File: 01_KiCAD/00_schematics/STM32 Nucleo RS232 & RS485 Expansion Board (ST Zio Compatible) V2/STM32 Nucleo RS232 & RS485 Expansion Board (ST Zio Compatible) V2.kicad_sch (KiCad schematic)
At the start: 0 parts

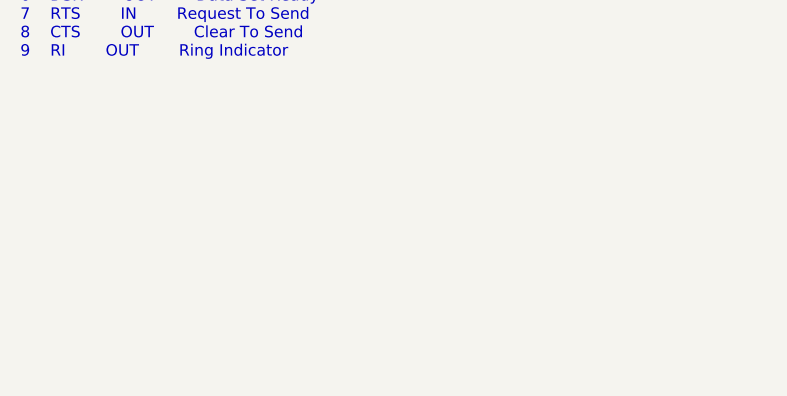
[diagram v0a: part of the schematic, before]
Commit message: Added components
Added R1 - R4 0R pass-through resistors for RS485 data lines to seperate them from RS232 Net
Added capacitors C1+ and C2+ for charge pump
Completed table on root page for THVD4431 and ZIO Connector Pin Layout
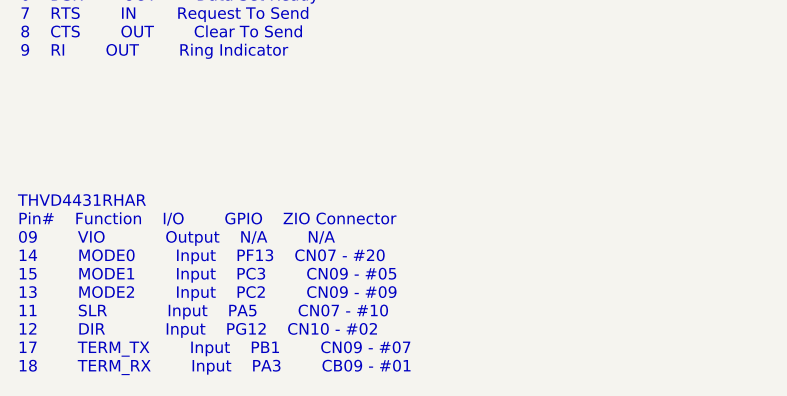
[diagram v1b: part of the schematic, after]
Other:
- note added: "THVD4431RHAR Pin# Function I/O GPIO ZIO Connector 09 VIO Output N/A N/A 14 MODE0 Input PF13 CN07 - #20 15 MODE1 Input PC3 CN09 - #05 13 MODE2 Input PC2 CN09 - #09 11 SLR Input PA5 CN07 - #10 12 DIR Input PG12 CN10 - #02 17 TERM_TX Input PB1 CN09 - #07 18 TERM_RX Input PA3 CB09 - #01"
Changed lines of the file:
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@@
+		)
+	)
+	(text "THVD4431RHAR\nPin#	Function	I/O		GPIO	ZIO Connector\n09		VIO			Output	N/A		N/A\n14		MODE0		Input	PF13	CN07 - #20\n15		MODE1		Input	PC3		CN09 - #05\n13		MODE2		Input	PC2		CN09 - #09\n11		SLR			Input	PA5		CN07 - #10\n12		DIR			Input	PG12	CN10 - #02\n17		TERM_TX		Input	PB1		CN09 - #07\n18		TERM_RX		Input	PA3		CB09 - #01\n"
+		(exclude_from_sim no)
+		(at 20.574 116.332 0)
+		(effects
+			(font
+				(size 1.27 1.27)
+			)
+			(justify left top)
 		)
 	)

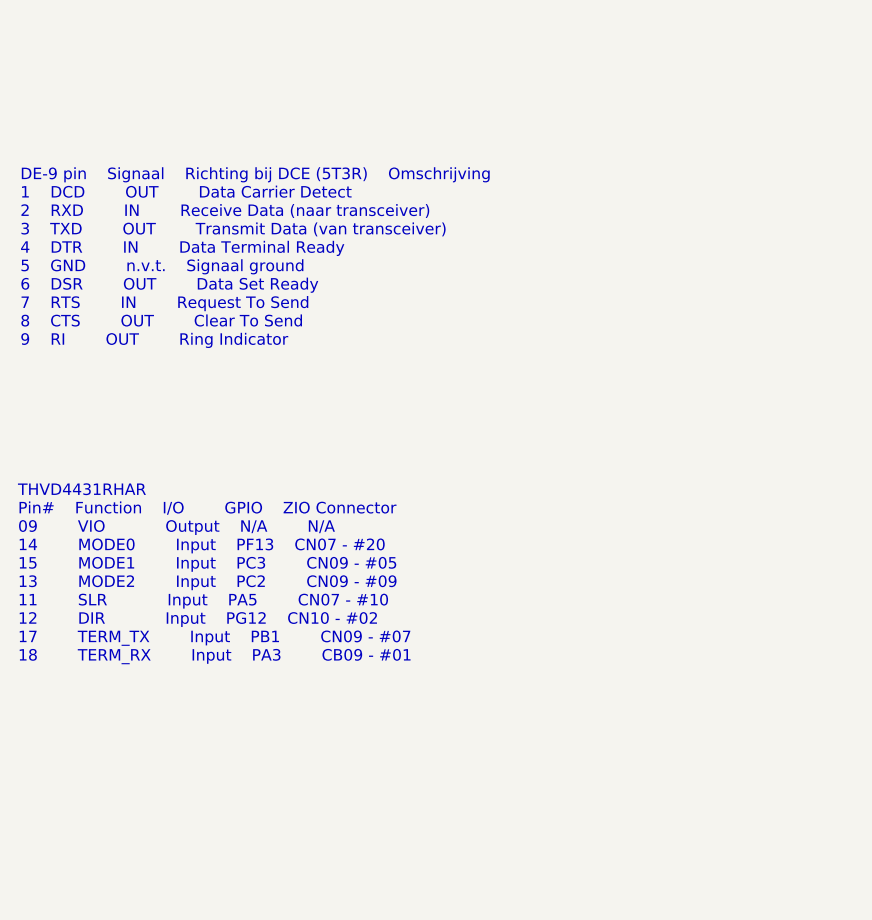
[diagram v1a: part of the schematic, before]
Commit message: Complemented descriptions
Complemented the RS232, RS485 and THVD4431 description table on the Root page
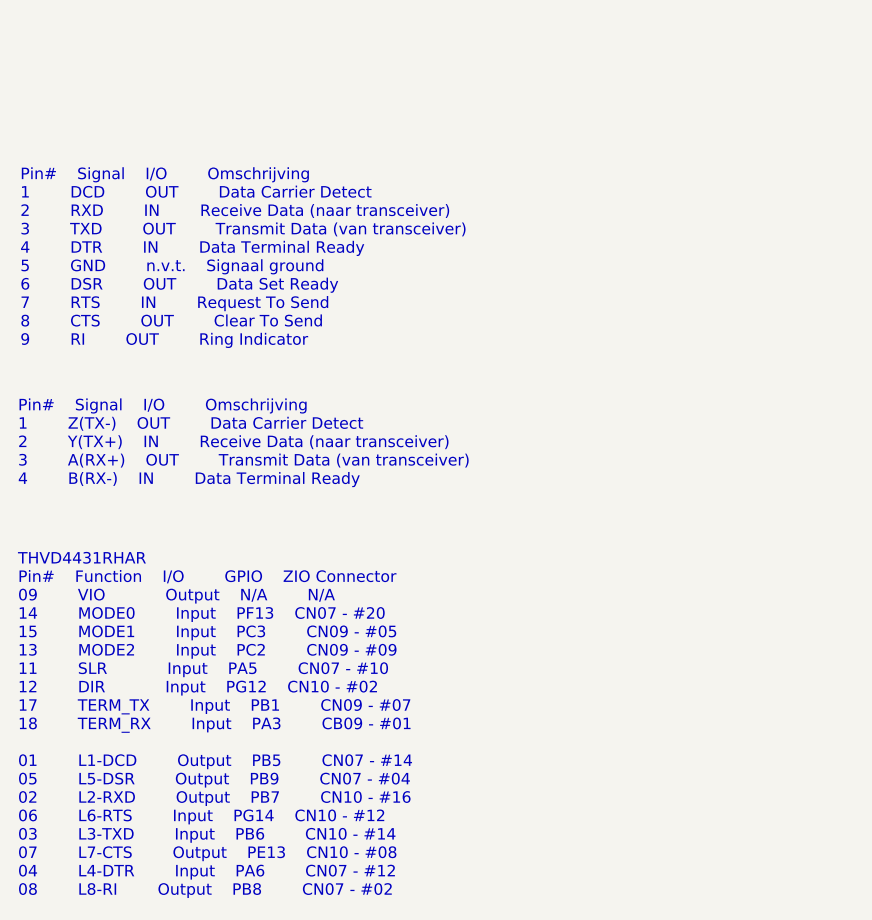
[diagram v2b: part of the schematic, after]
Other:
- note added: "Pin# Signal I/O Omschrijving 1 DCD OUT Data Carrier Detect 2 RXD IN Receive Data (naar transceiver) 3 TXD OUT Transmit Data (van transceiver) 4 DTR IN Data Terminal Ready 5 GND n.v.t. Signaal ground 6 DSR OUT Data Set Ready 7 RTS IN Request To Send 8 CTS OUT Clear To Send 9 RI OUT Ring Indicator"
- note added: "Pin# Signal I/O Omschrijving 1 Z(TX-) OUT Data Carrier Detect 2 Y(TX+) IN Receive Data (naar transceiver) 3 A(RX+) OUT Transmit Data (van transceiver) 4 B(RX-) IN Data Terminal Ready"
- note added: "THVD4431RHAR Pin# Function I/O GPIO ZIO Connector 09 VIO Output N/A N/A 14 MODE0 Input PF13 CN07 - #20 15 MODE1 Input PC3 CN09 - #05 13 MODE2 Input PC2 CN09 - #09 11 SLR Input PA5 CN07 - #10 12 DIR Input PG12 CN10 - #02 17 TERM_TX Input PB1 CN09 - #07 18 TERM_RX Input PA3 CB09 - #01 01 L1-DCD Output PB5 CN07 - #14 05 L5-DSR Output PB9 CN07 - #04 02 L2-RXD Output PB7 CN10 - #16 06 L6-RTS Input PG1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"
- note removed: "DE-9 pin Signaal Richting bij DCE (5T3R) Omschrijving 1 DCD OUT Data Carrier Detect 2 RXD IN Receive Data (naar transceiver) 3 TXD OUT Transmit Data (van transceiver) 4 DTR IN Data Terminal Ready 5 GND n.v.t. Signaal ground 6 DSR OUT Data Set Ready 7 RTS IN Request To Send 8 CTS OUT Clear To Send 9 RI OUT Ring Indicator"
- note removed: "THVD4431RHAR Pin# Function I/O GPIO ZIO Connector 09 VIO Output N/A N/A 14 MODE0 Input PF13 CN07 - #20 15 MODE1 Input PC3 CN09 - #05 13 MODE2 Input PC2 CN09 - #09 11 SLR Input PA5 CN07 - #10 12 DIR Input PG12 CN10 - #02 17 TERM_TX Input PB1 CN09 - #07 18 TERM_RX Input PA3 CB09 - #01"
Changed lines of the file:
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@@
 		(comment 3 "Initial revision")
 	)
-	(text "DE-9 pin	Signaal	Richting bij DCE (5T3R)	Omschrijving\n1	DCD		OUT		Data Carrier Detect\n2	RXD		IN		Receive Data (naar transceiver)\n3	TXD		OUT		Transmit Data (van transceiver)\n4	DTR		IN		Data Terminal Ready\n5	GND		n.v.t.	Signaal ground\n6	DSR		OUT		Data Set Ready\n7	RTS		IN		Request To Send\n8	CTS		OUT		Clear To Send\n9	RI		OUT		Ring Indicator"
+	(text "Pin#	Signal	I/O		Omschrijving\n1		DCD		OUT		Data Carrier Detect\n2		RXD		IN		Receive Data (naar transceiver)\n3		TXD		OUT		Transmit Data (van transceiver)\n4		DTR		IN		Data Terminal Ready\n5		GND		n.v.t.	Signaal ground\n6		DSR		OUT		Data Set Ready\n7		RTS		IN		Request To Send\n8		CTS		OUT		Clear To Send\n9		RI		OUT		Ring Indicator"
 		(exclude_from_sim no)
 		(at 20.828 91.186 0)
@@
 		)
 	)
-	(text "THVD4431RHAR\nPin#	Function	I/O		GPIO	ZIO Connector\n09		VIO			Output	N/A		N/A\n14		MODE0		Input	PF13	CN07 - #20\n15		MODE1		Input	PC3		CN09 - #05\n13		MODE2		Input	PC2		CN09 - #09\n11		SLR			Input	PA5		CN07 - #10\n12		DIR			Input	PG12	CN10 - #02\n17		TERM_TX		Input	PB1		CN09 - #07\n18		TERM_RX		Input	PA3		CB09 - #01\n"
+	(text "Pin#	Signal	I/O		Omschrijving\n1		Z(TX-)	OUT		Data Carrier Detect\n2		Y(TX+)	IN		Receive Data (naar transceiver)\n3		A(RX+)	OUT		Transmit Data (van transceiver)\n4		B(RX-)	IN		Data Terminal Ready\n"
 		(exclude_from_sim no)
-		(at 20.574 116.332 0)
+		(at 20.574 111.76 0)
 		(effects
 			(font
+				(size 1.27 1.27)
+			)
+			(justify left)
+		)
+	)
+	(text "THVD4431RHAR\nPin#	Function	I/O		GPIO	ZIO Connector\n09		VIO			Output	N/A		N/A\n14		MODE0		Input	PF13	CN07 - #20\n15		MODE1		Input	PC3		CN09 - #05\n13		MODE2		Input	PC2		CN09 - #09\n11		SLR			Input	PA5		CN07 - #10\n12		DIR			Input	PG12	CN10 - #02\n17		TERM_TX		Input	PB1		CN09 - #07\n18		TERM_RX		Input	PA3		CB09 - #01\n\n01		L1-DCD		Output	PB5		CN07 - #14\n05		L5-DSR		Output	PB9		CN07 - #04\n02		L2-RXD		Output	PB7		CN10 - #16\n06		L6-RTS		Input	PG14	CN10 - #12\n03		L3-TXD		Input	PB6		CN10 - #14\n07		L7-CTS		Output	PE13	CN10 - #08\n04		L4-DTR		Input	PA6		CN07 - #12\n08		L8-RI		Output	PB8		CN07 - #02"
+		(exclude_from_sim no)
+		(at 20.574 123.952 0)
+		(effects
+			(font

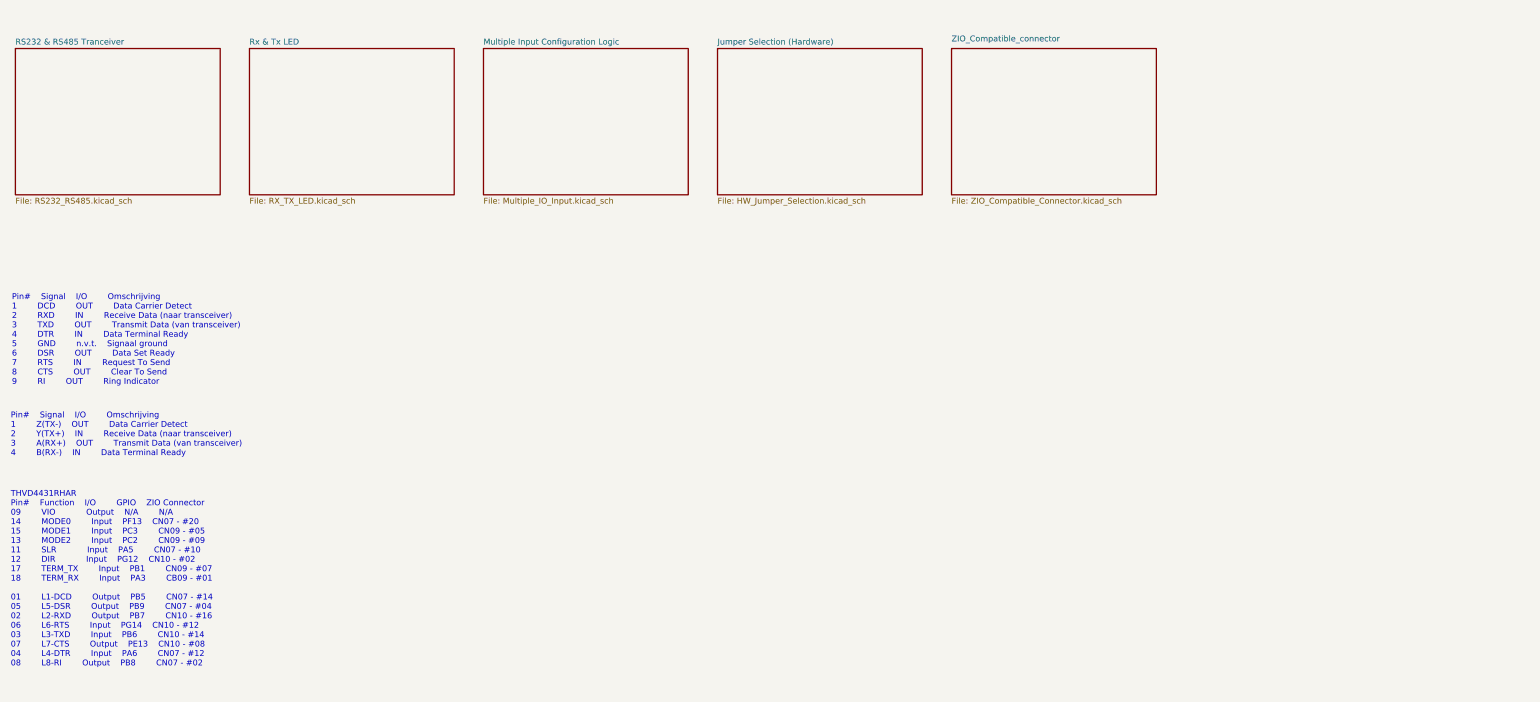
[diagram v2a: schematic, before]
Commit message: Added Dual Voltage Input
Added Dual Voltage Auto Select Input drawings. Added new hierarchical sheet with new pagenumber one. All other pages have been moved up by 1.
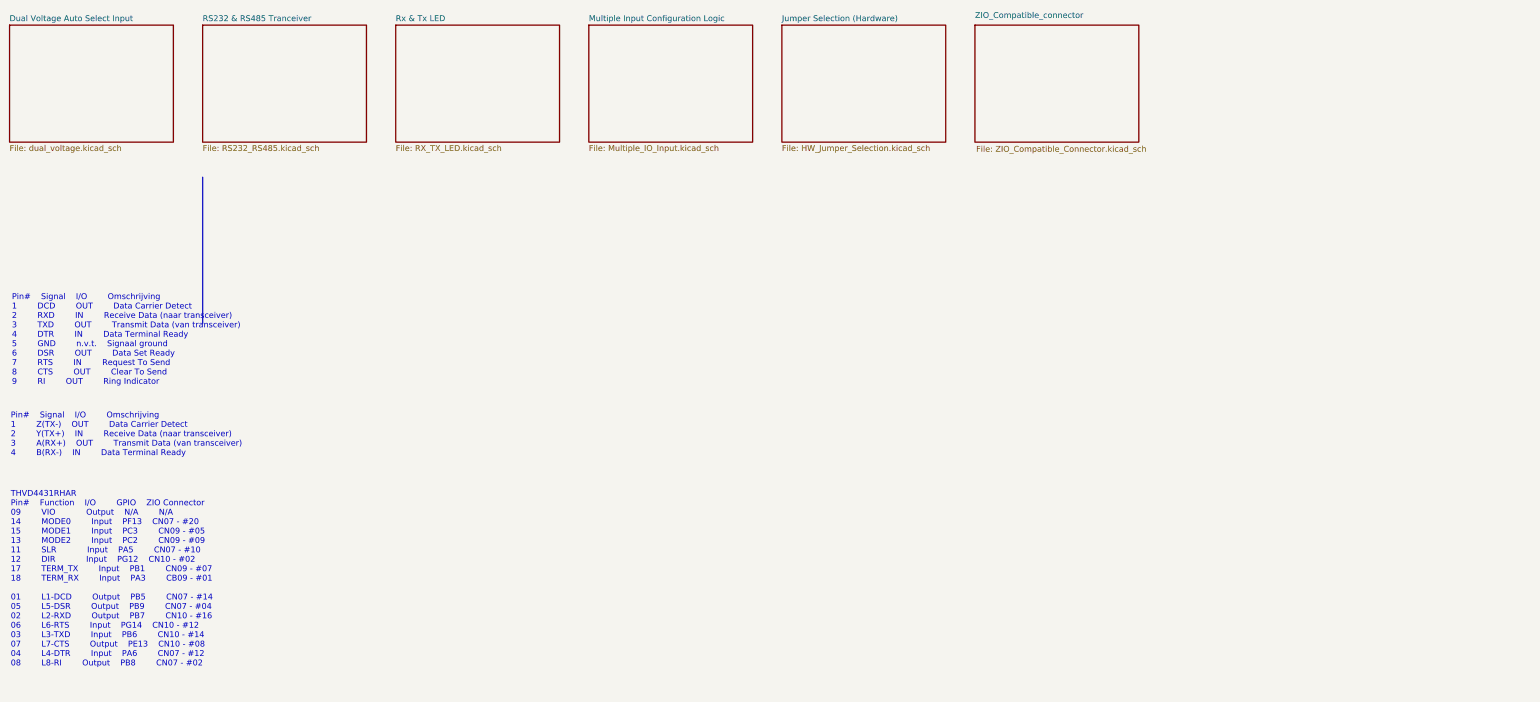
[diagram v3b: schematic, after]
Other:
- added sheet Dual Voltage Auto Select Input (dual_voltage.kicad_sch)
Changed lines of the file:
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@@
 		)
 	)
-	(sheet
-		(at 224.79 27.94)
-		(size 44.45 31.75)
+	(polyline
+		(pts
+			(xy 62.23 87.63) (xy 62.23 55.88)
+		)
+		(stroke
+			(width 0)
+			(type default)
+		)
+	)
+	(sheet
+		(at 229.87 22.86)
+		(size 35.56 25.4)
 		(exclude_from_sim no)
 		(in_bom yes)
@@
 		)
 		(property "Sheetname" "ZIO_Compatible_connector"
-			(at 224.79 26.543 0)
+			(at 229.87 21.463 0)
 			(effects
 				(font
@@
 		)
 		(property "Sheetfile" "ZIO_Compatible_Connector.kicad_sch"
-			(at 224.79 60.2746 0)
+			(at 230.124 49.022 0)
+			(effects
+				(font
+					(size 1.27 1.27)
+				)
+				(justify left top)
+			)
+		)
+		(instances
+			(project "STM32 Nucleo RS232 & RS485 Expansion Board (ST Zio Compatible) V2"
+				(path "/080f83b7-8913-48e8-ab8e-79cb12295542"
+					(page "7")
+				)
+			)
+		)
+	)
+	(sheet
+		(at 146.05 22.86)
+		(size 35.56 25.4)
+		(exclude_from_sim no)
+		(in_bom yes)
+		(on_board yes)
+		(dnp no)
+		(fields_autoplaced yes)
+		(stroke
+			(width 0.1524)
+			(type solid)
+		)
+		(fill
+			(color 0 0 0 0.0000)
+		)
+		(property "Sheetname" "Multiple Input Configuration Logic"
+			(at 146.05 22.1484 0)
+			(effects
+				(font
+					(size 1.27 1.27)
+				)
+				(justify left bottom)
+			)
+		)
+		(property "Sheetfile" "Multiple_IO_Input.kicad_sch"
+			(at 146.05 48.8446 0)
+			(effects
+				(font
+					(size 1.27 1.27)
+				)
+				(justify left top)
+			)
+		)
+		(instances
+			(project "STM32 Nucleo RS232 & RS485 Expansion Board (ST Zio Compatible) V2"
+				(path "/080f83b7-8913-48e8-ab8e-79cb12295542"
+					(page "5")
+				)
+			)
+		)
+	)
+	(sheet
+		(at 187.96 22.86)
+		(size 35.56 25.4)
+		(exclude_from_sim no)
+		(in_bom yes)
+		(on_board yes)
+		(dnp no)
+		(fields_autoplaced yes)
+		(stroke
+			(width 0.1524)
+			(type solid)
+		)
+		(fill
+			(color 0 0 0 0.0000)
+		)
+		(property "Sheetname" "Jumper Selection (Hardware)"
+			(at 187.96 22.1484 0)
+			(effects
+				(font
+					(size 1.27 1.27)
+				)
+				(justify left bottom)
+			)
+		)
+		(property "Sheetfile" "HW_Jumper_Selection.kicad_sch"
+			(at 187.96 48.8446 0)
 			(effects
 				(font
@@
 	)
 	(sheet
-		(at 123.19 27.94)
-		(size 44.45 31.75)
-		(exclude_from_sim no)
-		(in_bom yes)
-		(on_board yes)
-		(dnp no)
-		(fields_autoplaced yes)
-		(stroke
-			(width 0.1524)
-			(type solid)
-		)
-		(fill
-			(color 0 0 0 0.0000)
-		)
-		(property "Sheetname" "Multiple Input Configuration Logic"
-			(at 123.19 27.2284 0)
-			(effects
-				(font
-					(size 1.27 1.27)
-				)
-				(justify left bottom)
-			)
-		)
-		(property "Sheetfile" "Multiple_IO_Input.kicad_sch"
-			(at 123.19 60.2746 0)
+		(at 20.32 22.86)
+		(size 35.56 25.4)
+		(exclude_from_sim no)
+		(in_bom yes)
+		(on_board yes)
+		(dnp no)
+		(fields_autoplaced yes)
+		(stroke
+			(width 0.1524)
+			(type solid)
+		)
+		(fill
+			(color 0 0 0 0.0000)
+		)
+		(property "Sheetname" "Dual Voltage Auto Select Input"
+			(at 20.32 22.1484 0)
+			(effects
+				(font
+					(size 1.27 1.27)
+				)
+				(justify left bottom)
+			)
+		)
+		(property "Sheetfile" "dual_voltage.kicad_sch"
+			(at 20.32 48.8446 0)
+			(effects
+				(font
+					(size 1.27 1.27)
+				)
+				(justify left top)
+			)
+		)
+		(instances
+			(project "STM32 Nucleo RS232 & RS485 Expansion Board (ST Zio Compatible) V2"
+				(path "/080f83b7-8913-48e8-ab8e-79cb12295542"
+					(page "2")
+				)
+			)
+		)
+	)
+	(sheet
+		(at 104.14 22.86)
+		(size 35.56 25.4)
+		(exclude_from_sim no)
+		(in_bom yes)
+		(on_board yes)
+		(dnp no)
+		(fields_autoplaced yes)
+		(stroke
+			(width 0.1524)
+			(type solid)
+		)
+		(fill
+			(color 0 0 0 0.0000)
+		)
+		(property "Sheetname" "Rx & Tx LED"
+			(at 104.14 22.1484 0)
+			(effects
+				(font
+					(size 1.27 1.27)
+				)
+				(justify left bottom)
+			)
+		)
+		(property "Sheetfile" "RX_TX_LED.kicad_sch"
+			(at 104.14 48.8446 0)
 			(effects
 				(font
@@
 	)
 	(sheet
-		(at 173.99 27.94)
-		(size 44.45 31.75)
-		(exclude_from_sim no)
-		(in_bom yes)
-		(on_board yes)
-		(dnp no)
-		(fields_autoplaced yes)
-		(stroke
-			(width 0.1524)
-			(type solid)
-		)
-		(fill
-			(color 0 0 0 0.0000)
-		)
-		(property "Sheetname" "Jumper Selection (Hardware)"
-			(at 173.99 27.2284 0)
-			(effects
-				(font
-					(size 1.27 1.27)
-				)
-				(justify left bottom)
-			)
-		)
-		(property "Sheetfile" "HW_Jumper_Selection.kicad_sch"
-			(at 173.99 60.2746 0)
-			(effects
-				(font
-					(size 1.27 1.27)
-				)
-				(justify left top)
-			)
-		)
-		(instances
-			(project "STM32 Nucleo RS232 & RS485 Expansion Board (ST Zio Compatible) V2"
-				(path "/080f83b7-8913-48e8-ab8e-79cb12295542"
-					(page "5")
-				)
-			)
-		)
-	)
-	(sheet
-		(at 72.39 27.94)
-		(size 44.45 31.75)
-		(exclude_from_sim no)
-		(in_bom yes)
-		(on_board yes)
-		(dnp no)
-		(fields_autoplaced yes)
-		(stroke
-			(width 0.1524)
-			(type solid)
-		)
-		(fill
-			(color 0 0 0 0.0000)
-		)
-		(property "Sheetname" "Rx & Tx LED"
-			(at 72.39 27.2284 0)
-			(effects
-				(font
-					(size 1.27 1.27)
-				)
-				(justify left bottom)
-			)
-		)
-		(property "Sheetfile" "RX_TX_LED.kicad_sch"
-			(at 72.39 60.2746 0)
+		(at 62.23 22.86)
+		(size 35.56 25.4)
+		(exclude_from_sim no)
+		(in_bom yes)
+		(on_board yes)
+		(dnp no)
+		(fields_autoplaced yes)
+		(stroke
+			(width 0.1524)
+			(type solid)
+		)
+		(fill
+			(color 0 0 0 0.0000)
+		)
+		(property "Sheetname" "RS232 & RS485 Tranceiver"
+			(at 62.23 22.1484 0)
+			(effects
+				(font
+					(size 1.27 1.27)
+				)
+				(justify left bottom)
+			)
+		)
+		(property "Sheetfile" "RS232_RS485.kicad_sch"
+			(at 62.23 48.8446 0)
 			(effects
 				(font
@@
 				)
 			)
-		)
-	)
-	(sheet
-		(at 21.59 27.94)
-		(size 44.45 31.75)
-		(exclude_from_sim no)
-		(in_bom yes)
-		(on_board yes)
-		(dnp no)
-		(fields_autoplaced yes)
-		(stroke
-			(width 0.1524)
-			(type solid)
-		)
-		(fill
-			(color 0 0 0 0.0000)
-		)
-		(property "Sheetname" "RS232 & RS485 Tranceiver"
-			(at 21.59 27.2284 0)
-			(effects
-				(font
-					(size 1.27 1.27)
-				)
-				(justify left bottom)
-			)
-		)
-		(property "Sheetfile" "RS232_RS485.kicad_sch"
-			(at 21.59 60.2746 0)
-			(effects
-				(font
-					(size 1.27 1.27)
-				)
-				(justify left top)
-			)
-		)
-		(instances
-			(project "STM32 Nucleo RS232 & RS485 Expansion Board (ST Zio Compatible) V2"
-				(path "/080f83b7-8913-48e8-ab8e-79cb12295542"
-					(page "2")
-				)
-			)

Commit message: Finisching touches to schematics
Finalizing the schematics and double-check all connections throughout the different sheets.
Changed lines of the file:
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@@
 	(polyline
 		(pts
-			(xy 62.23 87.63) (xy 62.23 55.88)
+			(xy 91.44 91.44) (xy 91.44 59.69)
 		)
 		(stroke

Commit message: Finishing up the schematic aand created the board outline
Made some finishing touches to the schematic, updated all the symbol footprints and started to create the board.
Added missing 3D models for Phoenix 4-p RS485 connector and RS232 connector, also for Inolux LED.
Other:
- note added: "STANDAARD CONFIGURATIE: RS232, software disabled Jumper Hardware selection RS485 Termination on R1+R2 and R3+R4 both disabled (gnd) Slew Rate Control (SLR) set to slow speed"
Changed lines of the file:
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@@
 		)
 	)
-	(polyline
-		(pts
-			(xy 91.44 91.44) (xy 91.44 59.69)
-		)
-		(stroke
-			(width 0)
-			(type default)
+	(text "STANDAARD CONFIGURATIE:\n\nRS232, \nsoftware disabled\nJumper Hardware selection\nRS485 Termination on R1+R2 and R3+R4 both disabled (gnd)\nSlew Rate Control (SLR) set to slow speed"
+		(exclude_from_sim no)
+		(at 126.238 88.392 0)
+		(effects
+			(font
+				(size 1.27 1.27)
+			)
+			(justify left)
 		)
 	)

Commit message: Added half-duplex jumpers
Addres jumpers for hardware RS485 half-duplex configuration combining signals A(Y) & B(Z). Finalising testpoints and added 3D models for each test-point color.
-Green = logic side
-Blue = connector side
Made some minor changed to layout for test signals clarification (THVD4431 sheet)
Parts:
- added U6: NUCLEO-H753ZI, NUCLEO-H753ZI:MODULE_NUCLEO-H753ZI, symbol NUCLEO-H753ZI:NUCLEO-H753ZI

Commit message: Finalizing PCB Design
Finalizing track routing on PCB and run DRC. Made some minor silkscreen adjustments.
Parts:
- removed U6: NUCLEO-H753ZI, NUCLEO-H753ZI:MODULE_NUCLEO-H753ZI, symbol NUCLEO-H753ZI:NUCLEO-H753ZI
